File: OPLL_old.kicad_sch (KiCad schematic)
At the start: 56 parts, among them J1 Conn_Coaxial, J2 Conn_Coaxial, J3 B4B-PH-K-S_LF__SN_, J4 Conn_Coaxial, J5 Conn_Coaxial, J6 Conn_Coaxial, J7 OSTTC042162, U1 ADF4107, U2 Opamp_Quad, U3 OPA847xDBV, U4 MC7805CD2TR4G D+, U5 MC7805CD2TR4G A+, U6 MC7905ACD2TR4G A-, U7 LP2950ACDT-3.3RG

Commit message: First OPLL iteration
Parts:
- added H1, H2: MountingHole, MountingHole:MountingHole_3.2mm_M3, symbol Mechanical:MountingHole
- D2, D3: renamed from D?; value 1.5KExxA -> SA15CA-TP
- F1, F2: renamed from F?; value Polyfuse -> Polyfuse RXEF040; footprint (none) -> Fuse:Fuse_BelFuse_0ZRE0005FF_L8.3mm_W3.8mm
- gave numbers to parts that had none: 1
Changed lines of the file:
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@@
   )
   (symbol (lib_id "Device:Polyfuse") (at 195.58 78.74 0) (unit 1)
-    (in_bom yes) (on_board yes) (fields_autoplaced)
-    (property "Reference" "F?" (id 0) (at 198.12 77.4699 0)
-      (effects (font (size 1.27 1.27)) (justify left))
-    )
-    (property "Value" "Polyfuse" (id 1) (at 198.12 80.0099 0)
-      (effects (font (size 1.27 1.27)) (justify left))
-    )
-    (property "Footprint" "" (id 2) (at 196.85 83.82 0)
+    (in_bom yes) (on_board yes)
+    (property "Reference" "F1" (id 0) (at 198.12 77.4699 0)
+      (effects (font (size 1.27 1.27)) (justify left))
+    )
+    (property "Value" "Polyfuse RXEF040" (id 1) (at 186.69 83.82 0)
+      (effects (font (size 1.27 1.27)) (justify left))
+    )
+    (property "Footprint" "Fuse:Fuse_BelFuse_0ZRE0005FF_L8.3mm_W3.8mm" (id 2) (at 196.85 83.82 0)
       (effects (font (size 1.27 1.27)) (justify left) hide)
     )
@@
   (symbol (lib_id "Device:Polyfuse") (at 205.74 78.74 0) (unit 1)
     (in_bom yes) (on_board yes) (fields_autoplaced)
-    (property "Reference" "F?" (id 0) (at 208.28 77.4699 0)
-      (effects (font (size 1.27 1.27)) (justify left))
-    )
-    (property "Value" "Polyfuse" (id 1) (at 208.28 80.0099 0)
-      (effects (font (size 1.27 1.27)) (justify left))
-    )
-    (property "Footprint" "" (id 2) (at 207.01 83.82 0)
+    (property "Reference" "F2" (id 0) (at 208.28 77.4699 0)
+      (effects (font (size 1.27 1.27)) (justify left))
+    )
+    (property "Value" "Polyfuse RXEF040" (id 1) (at 208.28 80.0099 0)
+      (effects (font (size 1.27 1.27)) (justify left))
+    )
+    (property "Footprint" "Fuse:Fuse_BelFuse_0ZRE0005FF_L8.3mm_W3.8mm" (id 2) (at 207.01 83.82 0)
       (effects (font (size 1.27 1.27)) (justify left) hide)
     )
@@
     (pin "4")
   )
+  (symbol (lib_id "Mechanical:MountingHole") (at 260.35 39.37 0) (unit 1)
+    (in_bom yes) (on_board yes) (fields_autoplaced)
+    (property "Reference" "H2" (id 0) (at 262.89 38.0999 0)
+      (effects (font (size 1.27 1.27)) (justify left))
+    )
+    (property "Value" "MountingHole" (id 1) (at 262.89 40.6399 0)
+      (effects (font (size 1.27 1.27)) (justify left))
+    )
+    (property "Footprint" "MountingHole:MountingHole_3.2mm_M3" (id 2) (at 260.35 39.37 0)
+      (effects (font (size 1.27 1.27)) hide)
+    )
+    (property "Datasheet" "~" (id 3) (at 260.35 39.37 0)
+      (effects (font (size 1.27 1.27)) hide)
+    )
+  )
   (symbol (lib_id "Device:R") (at 313.69 191.77 0) (unit 1)
     (in_bom yes) (on_board yes)
@@
   (symbol (lib_id "Device:C_Polarized_Small_US") (at 191.77 68.58 0) (unit 1)
     (in_bom yes) (on_board yes)
-    (property "Reference" "C?" (id 0) (at 194.31 66.8781 0)
+    (property "Reference" "C13" (id 0) (at 194.31 66.8781 0)
       (effects (font (size 1.27 1.27)) (justify left))
     )
@@
   (symbol (lib_id "power:GND2") (at 200.66 62.23 180) (unit 1)
     (in_bom yes) (on_board yes)
-    (property "Reference" "#PWR?" (id 0) (at 200.66 55.88 0)
+    (property "Reference" "#PWR0149" (id 0) (at 200.66 55.88 0)
       (effects (font (size 1.27 1.27)) hide)
     )
@@
   (symbol (lib_id "Diode:1.5KExxA") (at 214.63 67.31 90) (unit 1)
     (in_bom yes) (on_board yes) (fields_autoplaced)
-    (property "Reference" "D?" (id 0) (at 217.17 66.0399 90)
+    (property "Reference" "D3" (id 0) (at 217.17 66.0399 90)
       (effects (font (size 1.27 1.27)) (justify right))
     )
-    (property "Value" "1.5KExxA" (id 1) (at 217.17 68.5799 90)
+    (property "Value" "SA15CA-TP" (id 1) (at 217.17 68.5799 90)
       (effects (font (size 1.27 1.27)) (justify right))
     )
@@
   (symbol (lib_id "Diode:1.5KExxA") (at 185.42 67.31 90) (unit 1)
     (in_bom yes) (on_board yes)
-    (property "Reference" "D?" (id 0) (at 176.53 64.77 90)
+    (property "Reference" "D2" (id 0) (at 176.53 64.77 90)
       (effects (font (size 1.27 1.27)) (justify right))
     )
-    (property "Value" "1.5KExxA" (id 1) (at 172.72 67.31 90)
+    (property "Value" "SA15CA-TP" (id 1) (at 172.72 67.31 90)
       (effects (font (size 1.27 1.27)) (justify right))
     )
@@
     (pin "1")
     (pin "2")
+  )
+  (symbol (lib_id "Mechanical:MountingHole") (at 238.76 39.37 0) (unit 1)
+    (in_bom yes) (on_board yes) (fields_autoplaced)
+    (property "Reference" "H1" (id 0) (at 241.3 38.0999 0)
+      (effects (font (size 1.27 1.27)) (justify left))
+    )
+    (property "Value" "MountingHole" (id 1) (at 241.3 40.6399 0)
+      (effects (font (size 1.27 1.27)) (justify left))
+    )
+    (property "Footprint" "MountingHole:MountingHole_3.2mm_M3" (id 2) (at 238.76 39.37 0)
+      (effects (font (size 1.27 1.27)) hide)
+    )
+    (property "Datasheet" "~" (id 3) (at 238.76 39.37 0)
+      (effects (font (size 1.27 1.27)) hide)
+    )
   )
   (symbol (lib_id "power:-15V") (at 214.63 71.12 180) (unit 1)
@@
     )
     (path "/b573a6c6-283d-4db4-baa9-6c697948bbe1"
-      (reference "#PWR?") (unit 1) (value "GND2") (footprint "")
+      (reference "#PWR0149") (unit 1) (value "GND2") (footprint "")
     )
     (path "/4306b6a0-1fb8-409b-b7a8-c7635879765f"
@@
     )
     (path "/b18589d6-3fe0-4adc-a013-dac50eab74ad"
-      (reference "C?") (unit 1) (value "C_Polarized_Small_US") (footprint "Capacitor_THT:CP_Radial_D10.0mm_P5.00mm")
+      (reference "C13") (unit 1) (value "C_Polarized_Small_US") (footprint "Capacitor_THT:CP_Radial_D10.0mm_P5.00mm")
     )
     (path "/0d701ffd-2f7c-40b3-90ae-5e7206d649b0"
       (reference "D1") (unit 1) (value " XLMDKVG58M") (footprint "digikey-footprints:LED_5mm_Radial")
     )
+    (path "/f626d05c-395e-4220-a862-f0832a775d16"
+      (reference "D2") (unit 1) (value "SA15CA-TP") (footprint "Diode_THT:D_DO-201AE_P15.24mm_Horizontal")
+    )
     (path "/d684ce3c-f235-4e5e-b764-eeef7bd4d9c4"
-      (reference "D?") (unit 1) (value "1.5KExxA") (footprint "Diode_THT:D_DO-201AE_P15.24mm_Horizontal")
-    )
-    (path "/f626d05c-395e-4220-a862-f0832a775d16"
-      (reference "D?") (unit 1) (value "1.5KExxA") (footprint "Diode_THT:D_DO-201AE_P15.24mm_Horizontal")
+      (reference "D3") (unit 1) (value "SA15CA-TP") (footprint "Diode_THT:D_DO-201AE_P15.24mm_Horizontal")
     )
     (path "/2296a51b-2641-47e0-b134-d9d95b87a65b"
-      (reference "F?") (unit 1) (value "Polyfuse") (footprint "")
+      (reference "F1") (unit 1) (value "Polyfuse RXEF040") (footprint "Fuse:Fuse_BelFuse_0ZRE0005FF_L8.3mm_W3.8mm")
     )
     (path "/2d75a830-52fb-41bc-9956-df753cb91f7f"
-      (reference "F?") (unit 1) (value "Polyfuse") (footprint "")
+      (reference "F2") (unit 1) (value "Polyfuse RXEF040") (footprint "Fuse:Fuse_BelFuse_0ZRE0005FF_L8.3mm_W3.8mm")
+    )
+    (path "/f6ed1af7-a554-4762-b65f-178e225b2442"
+      (reference "H1") (unit 1) (value "MountingHole") (footprint "MountingHole:MountingHole_3.2mm_M3")
+    )
+    (path "/4bdd02b7-e82a-45e6-aa9b-c22beb653961"
+      (reference "H2") (unit 1) (value "MountingHole") (footprint "MountingHole:MountingHole_3.2mm_M3")
     )
     (path "/04df1c87-0d0f-4614-bf7a-2282be5beeeb"

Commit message: it2
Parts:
- removed J3: B4B-PH-K-S_LF__SN_, digikey-footprints:PinHeader_1x4_P2mm_Drill1mm, symbol dk_Rectangular-Connectors-Headers-Male-Pins:B4B-PH-K-S_LF__SN_
- added C14, C16: 10p, Capacitor_SMD:C_0402_1005Metric, symbol Device:C_Small
- added C15: 0.1u, Capacitor_SMD:C_0402_1005Metric, symbol Device:C_Small
- added C17, C18, C19, C20, C21, C22, C23, C24, C25, C26: T58W9105M035C0500, Capacitor_SMD:C_0805_2012Metric_Pad1.18x1.45mm_HandSolder, symbol Device:C_Polarized_Small_US
- added J3: OSTTC050162, digikey-footprints:Term_Block_1x5_P5mm, symbol dk_Terminal-Blocks-Wire-to-Board:OSTTC050162
- C10, C11: value 100p -> 0.1u
- C9: value 100p -> 10p
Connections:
- net +15V: now also C13.1, C17.1, C21.1; no longer C13.2
- net +3V3: now also C10.1, C15.1, C16.1, C20.1; no longer C10.2
- net +5VA: now also C23.1, C25.2
- net +5VD: now also C11.1, C14.1, C18.1, C19.1; no longer C11.2
- net -15V: now also C12.2, D3.2 (A2), C22.2; no longer C12.1, D3.1 (A1)
- net -5VA: now also C24.2, C26.1
- net at F1.2: now also J7.2; no longer J7.3
- net at U1.10 (CE): now also J3.2
- net at U1.11 (CLK): now also J3.3
- net at U1.12 (DATA): now also J3.4
- net at U1.13 (LE): now also J3.5
- net GND1 renamed GND
- net GND: now also C10.2, C11.2, C12.1, C13.2, C5.1, C6.1, D1.2 (AK), D2.2 (A2), D3.1 (A1), J4.2 (Ext), J5.2 (Ext), J6.2 (Ext), J7.1, J7.3, R10.1, R15.1, R19.2, R21.2, R4.2, R7.2, RV1.3, U1.3 (CPGND), U2.11 (-), U2.5 (+), U5.2 (GND), U6.2 (VI), C14.2, C15.2, C16.2, C17.2, C18.2, C19.2, C20.2, C21.2, C22.1, C23.2, C24.1, C25.1, C26.2, J3.1; no longer C10.1, C11.1, J7.2
- removed net GND2: C12.2, C13.1, C5.1, C6.1, D1.2 (AK), D2.2 (A2), D3.2 (A2), J4.2 (Ext), J5.2 (Ext), J6.2 (Ext), J7.1, R10.1, R15.1, R19.2, R21.2, R4.2, R7.2, RV1.3, U1.3 (CPGND), U2.11 (-), U2.5 (+), U5.2 (VI), U6.2 (VI)
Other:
- moved on the sheet: C12, C13, C9, D3

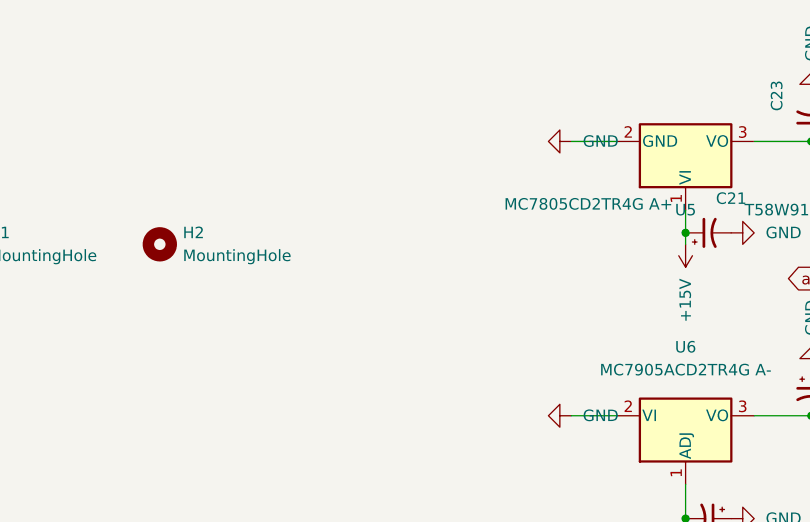
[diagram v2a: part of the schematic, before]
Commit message: FET update
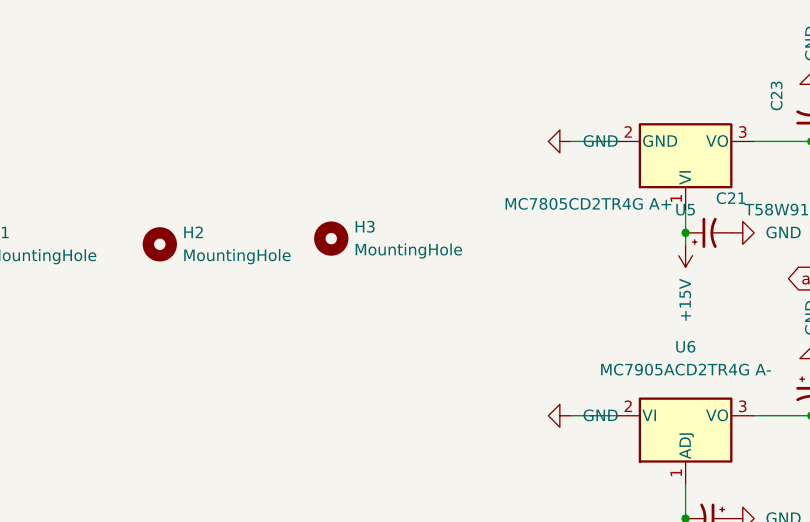
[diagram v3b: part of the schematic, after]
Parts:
- added H3: MountingHole, MountingHole:MountingHole_3.2mm_M3, symbol Mechanical:MountingHole
- C17, C18, C19, C20, C21, C22, C23, C24, C25, C26: footprint Capacitor_SMD:C_0805_2012Metric_Pad1.18x1.45mm_HandSolder -> Capacitor_SMD:C_1206_3216Metric_Pad1.33x1.80mm_HandSolder
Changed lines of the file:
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@@
     (property "Reference" "C21" (id 0) (at 323.85 34.29 90))
     (property "Value" "T58W9105M035C0500" (id 1) (at 335.28 35.56 90))
-    (property "Footprint" "Capacitor_SMD:C_0805_2012Metric_Pad1.18x1.45mm_HandSolder" (id 2) (at 321.31 38.1 0)
+    (property "Footprint" "Capacitor_SMD:C_1206_3216Metric_Pad1.33x1.80mm_HandSolder" (id 2) (at 321.31 38.1 0)
       (effects (font (size 1.27 1.27)) hide)
     )
@@
     (property "Reference" "C20" (id 0) (at 77.47 74.4982 90))
     (property "Value" "T58W9105M035C0500" (id 1) (at 74.93 88.9 90))
-    (property "Footprint" "Capacitor_SMD:C_0805_2012Metric_Pad1.18x1.45mm_HandSolder" (id 2) (at 71.12 74.93 0)
+    (property "Footprint" "Capacitor_SMD:C_1206_3216Metric_Pad1.33x1.80mm_HandSolder" (id 2) (at 71.12 74.93 0)
       (effects (font (size 1.27 1.27)) hide)
     )
@@
       (effects (font (size 1.524 1.524)) (justify left) hide)
     )
-    (pin "2")
-    (pin "5")
+    (pin "1")
+    (pin "2")
     (pin "3")
     (pin "4")
-    (pin "1")
+    (pin "5")
   )
   (symbol (lib_id "Device:R") (at 302.26 175.26 0) (unit 1)
@@
     (property "Reference" "C18" (id 0) (at 44.45 70.2818 90))
     (property "Value" "T58W9105M035C0500" (id 1) (at 46.99 60.96 90))
-    (property "Footprint" "Capacitor_SMD:C_0805_2012Metric_Pad1.18x1.45mm_HandSolder" (id 2) (at 50.8 69.85 0)
+    (property "Footprint" "Capacitor_SMD:C_1206_3216Metric_Pad1.33x1.80mm_HandSolder" (id 2) (at 50.8 69.85 0)
       (effects (font (size 1.27 1.27)) hide)
     )
@@
     (property "Reference" "C25" (id 0) (at 226.06 114.7318 90))
     (property "Value" "T58W9105M035C0500" (id 1) (at 228.6 100.33 90))
-    (property "Footprint" "Capacitor_SMD:C_0805_2012Metric_Pad1.18x1.45mm_HandSolder" (id 2) (at 232.41 114.3 0)
+    (property "Footprint" "Capacitor_SMD:C_1206_3216Metric_Pad1.33x1.80mm_HandSolder" (id 2) (at 232.41 114.3 0)
       (effects (font (size 1.27 1.27)) hide)
     )
@@
     (property "Reference" "C24" (id 0) (at 336.55 58.42 90))
     (property "Value" "T58W9105M035C0500" (id 1) (at 347.98 51.435 0))
-    (property "Footprint" "Capacitor_SMD:C_0805_2012Metric_Pad1.18x1.45mm_HandSolder" (id 2) (at 332.74 55.88 0)
+    (property "Footprint" "Capacitor_SMD:C_1206_3216Metric_Pad1.33x1.80mm_HandSolder" (id 2) (at 332.74 55.88 0)
       (effects (font (size 1.27 1.27)) hide)
     )
@@
     (property "Reference" "C19" (id 0) (at 58.42 77.47 90))
     (property "Value" "T58W9105M035C0500" (id 1) (at 49.53 86.36 90))
-    (property "Footprint" "Capacitor_SMD:C_0805_2012Metric_Pad1.18x1.45mm_HandSolder" (id 2) (at 54.61 74.93 0)
+    (property "Footprint" "Capacitor_SMD:C_1206_3216Metric_Pad1.33x1.80mm_HandSolder" (id 2) (at 54.61 74.93 0)
       (effects (font (size 1.27 1.27)) hide)
     )
@@
     (property "Reference" "C22" (id 0) (at 318.77 73.66 90))
     (property "Value" "T58W9105M035C0500" (id 1) (at 332.74 77.47 90))
-    (property "Footprint" "Capacitor_SMD:C_0805_2012Metric_Pad1.18x1.45mm_HandSolder" (id 2) (at 321.31 69.85 0)
+    (property "Footprint" "Capacitor_SMD:C_1206_3216Metric_Pad1.33x1.80mm_HandSolder" (id 2) (at 321.31 69.85 0)
       (effects (font (size 1.27 1.27)) hide)
     )
@@
     )
     (pin "1")
+  )
+  (symbol (lib_id "Mechanical:MountingHole") (at 279.4 38.735 0) (unit 1)
+    (in_bom yes) (on_board yes) (fields_autoplaced)
+    (property "Reference" "H3" (id 0) (at 281.94 37.4649 0)
+      (effects (font (size 1.27 1.27)) (justify left))
+    )
+    (property "Value" "MountingHole" (id 1) (at 281.94 40.0049 0)
+      (effects (font (size 1.27 1.27)) (justify left))
+    )
+    (property "Footprint" "MountingHole:MountingHole_3.2mm_M3" (id 2) (at 279.4 38.735 0)
+      (effects (font (size 1.27 1.27)) hide)
+    )
+    (property "Datasheet" "~" (id 3) (at 279.4 38.735 0)
+      (effects (font (size 1.27 1.27)) hide)
+    )
   )
   (symbol (lib_id "Device:Opamp_Quad") (at 154.94 147.32 0) (unit 1)
@@
     (property "Reference" "C26" (id 0) (at 254 113.8682 90))
     (property "Value" "T58W9105M035C0500" (id 1) (at 251.46 128.27 90))
-    (property "Footprint" "Capacitor_SMD:C_0805_2012Metric_Pad1.18x1.45mm_HandSolder" (id 2) (at 247.65 114.3 0)
+    (property "Footprint" "Capacitor_SMD:C_1206_3216Metric_Pad1.33x1.80mm_HandSolder" (id 2) (at 247.65 114.3 0)
       (effects (font (size 1.27 1.27)) hide)
     )
@@
     (property "Reference" "C23" (id 0) (at 328.93 22.86 90))
     (property "Value" "T58W9105M035C0500" (id 1) (at 344.805 21.59 0))
-    (property "Footprint" "Capacitor_SMD:C_0805_2012Metric_Pad1.18x1.45mm_HandSolder" (id 2) (at 332.74 25.4 0)
+    (property "Footprint" "Capacitor_SMD:C_1206_3216Metric_Pad1.33x1.80mm_HandSolder" (id 2) (at 332.74 25.4 0)
       (effects (font (size 1.27 1.27)) hide)
     )
@@
     (property "Reference" "C17" (id 0) (at 43.18 81.28 90))
     (property "Value" "T58W9105M035C0500" (id 1) (at 52.07 90.17 90))
-    (property "Footprint" "Capacitor_SMD:C_0805_2012Metric_Pad1.18x1.45mm_HandSolder" (id 2) (at 40.64 85.09 0)
+    (property "Footprint" "Capacitor_SMD:C_1206_3216Metric_Pad1.33x1.80mm_HandSolder" (id 2) (at 40.64 85.09 0)
       (effects (font (size 1.27 1.27)) hide)
     )
@@
     )
     (path "/fe5f4098-c47c-4492-be3c-e593ff207562"
-      (reference "C17") (unit 1) (value "T58W9105M035C0500") (footprint "Capacitor_SMD:C_0805_2012Metric_Pad1.18x1.45mm_HandSolder")
+      (reference "C17") (unit 1) (value "T58W9105M035C0500") (footprint "Capacitor_SMD:C_1206_3216Metric_Pad1.33x1.80mm_HandSolder")
     )
     (path "/3ee645d9-3f70-4550-b535-b756b30b618d"
-      (reference "C18") (unit 1) (value "T58W9105M035C0500") (footprint "Capacitor_SMD:C_0805_2012Metric_Pad1.18x1.45mm_HandSolder")
+      (reference "C18") (unit 1) (value "T58W9105M035C0500") (footprint "Capacitor_SMD:C_1206_3216Metric_Pad1.33x1.80mm_HandSolder")
     )
     (path "/7808e665-1c83-4ca4-9707-8893ef3a81af"
-      (reference "C19") (unit 1) (value "T58W9105M035C0500") (footprint "Capacitor_SMD:C_0805_2012Metric_Pad1.18x1.45mm_HandSolder")
+      (reference "C19") (unit 1) (value "T58W9105M035C0500") (footprint "Capacitor_SMD:C_1206_3216Metric_Pad1.33x1.80mm_HandSolder")
     )
     (path "/07ce28bf-4982-4ea6-bd84-364cb9ef446b"
-      (reference "C20") (unit 1) (value "T58W9105M035C0500") (footprint "Capacitor_SMD:C_0805_2012Metric_Pad1.18x1.45mm_HandSolder")
+      (reference "C20") (unit 1) (value "T58W9105M035C0500") (footprint "Capacitor_SMD:C_1206_3216Metric_Pad1.33x1.80mm_HandSolder")
     )
     (path "/0611792e-2fbb-4eba-ab1f-da572f6bd614"
-      (reference "C21") (unit 1) (value "T58W9105M035C0500") (footprint "Capacitor_SMD:C_0805_2012Metric_Pad1.18x1.45mm_HandSolder")
+      (reference "C21") (unit 1) (value "T58W9105M035C0500") (footprint "Capacitor_SMD:C_1206_3216Metric_Pad1.33x1.80mm_HandSolder")
     )
     (path "/c1c70994-9515-48e6-830a-30dba481382a"
-      (reference "C22") (unit 1) (value "T58W9105M035C0500") (footprint "Capacitor_SMD:C_0805_2012Metric_Pad1.18x1.45mm_HandSolder")
+      (reference "C22") (unit 1) (value "T58W9105M035C0500") (footprint "Capacitor_SMD:C_1206_3216Metric_Pad1.33x1.80mm_HandSolder")
     )
     (path "/fde8c4ce-00af-4a9c-9ce7-33d5946a6294"
-      (reference "C23") (unit 1) (value "T58W9105M035C0500") (footprint "Capacitor_SMD:C_0805_2012Metric_Pad1.18x1.45mm_HandSolder")
+      (reference "C23") (unit 1) (value "T58W9105M035C0500") (footprint "Capacitor_SMD:C_1206_3216Metric_Pad1.33x1.80mm_HandSolder")
     )
     (path "/5c09ed37-7d01-4346-8d1e-27cf5bc85cca"
-      (reference "C24") (unit 1) (value "T58W9105M035C0500") (footprint "Capacitor_SMD:C_0805_2012Metric_Pad1.18x1.45mm_HandSolder")
+      (reference "C24") (unit 1) (value "T58W9105M035C0500") (footprint "Capacitor_SMD:C_1206_3216Metric_Pad1.33x1.80mm_HandSolder")
     )
     (path "/5badb923-6964-4d2f-a90b-8d5a7f60926e"
-      (reference "C25") (unit 1) (value "T58W9105M035C0500") (footprint "Capacitor_SMD:C_0805_2012Metric_Pad1.18x1.45mm_HandSolder")
+      (reference "C25") (unit 1) (value "T58W9105M035C0500") (footprint "Capacitor_SMD:C_1206_3216Metric_Pad1.33x1.80mm_HandSolder")
     )
     (path "/f67d7bb6-ac39-4a63-a6e8-b59f244b3e8f"
-      (reference "C26") (unit 1) (value "T58W9105M035C0500") (footprint "Capacitor_SMD:C_0805_2012Metric_Pad1.18x1.45mm_HandSolder")
+      (reference "C26") (unit 1) (value "T58W9105M035C0500") (footprint "Capacitor_SMD:C_1206_3216Metric_Pad1.33x1.80mm_HandSolder")
     )
     (path "/0d701ffd-2f7c-40b3-90ae-5e7206d649b0"
@@
       (reference "H2") (unit 1) (value "MountingHole") (footprint "MountingHole:MountingHole_3.2mm_M3")
     )
+    (path "/e04eb504-5e7a-4a39-852a-38df0fd7a84f"
+      (reference "H3") (unit 1) (value "MountingHole") (footprint "MountingHole:MountingHole_3.2mm_M3")
+    )
     (path "/04df1c87-0d0f-4614-bf7a-2282be5beeeb"
